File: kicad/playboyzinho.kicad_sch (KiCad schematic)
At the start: 17 parts, among them SW1 SW_Push, SW2 SW_Push, SW3 SW_Push, SW4 SW_Push, SW5 SW_Push, SW6 SW_Push, SW7 SW_Push, SW8 SW_Push, SW9 SW_SPDT, U1 esp32-s3-pl, U7 (amplificador)_MAX98357_Module

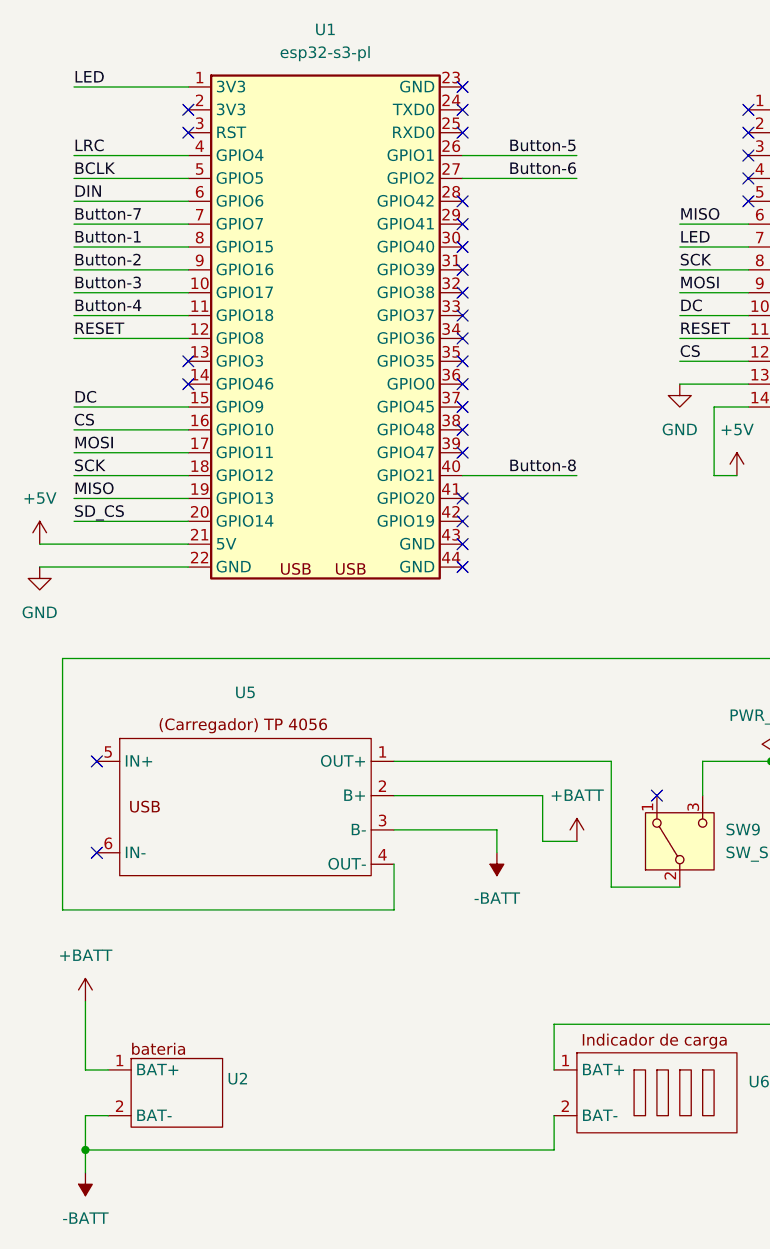
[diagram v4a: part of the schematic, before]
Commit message: refact: altera posição dos pinos dos botões e associa corretamente os footprints na parte de símbolos (antes, estava só no esquemático)
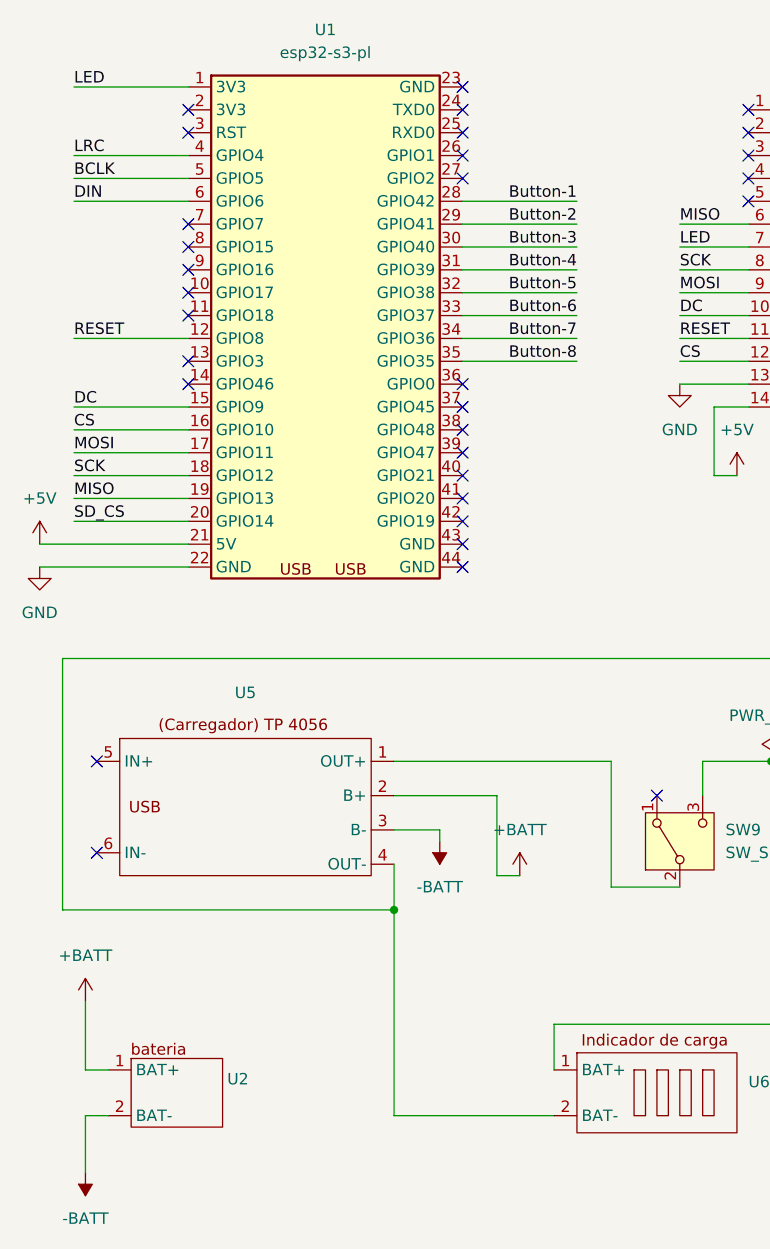
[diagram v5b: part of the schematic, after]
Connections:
- net -BATT: no longer U6.2 (BAT-)
- net Button-1: now also U1.28 (GPIO42); no longer U1.8 (GPIO15)
- net Button-2: now also U1.29 (GPIO41); no longer U1.9 (GPIO16)
- net Button-3: now also U1.30 (GPIO40); no longer U1.10 (GPIO17)
- net Button-4: now also U1.31 (GPIO39); no longer U1.11 (GPIO18)
- net Button-5: now also U1.32 (GPIO38); no longer U1.26 (GPIO1)
- net Button-6: now also U1.33 (GPIO37); no longer U1.27 (GPIO2)
- net Button-7: now also U1.34 (GPIO36); no longer U1.7 (GPIO7)
- net Button-8: now also U1.35 (GPIO35); no longer U1.40 (GPIO21)
- net at U3.4 (VIN-), U5.4 (OUT-): now also U6.2 (BAT-)

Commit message: feat: finaliza pcb
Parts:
- removed U6: (no value), lib-do-playboy:indicador-bateria, symbol lib-do-playboy:Indicador-Bateria
- added U6: (no value), lib-do-playboy:indicador-bateria, symbol lib-do-playboy:indicador-bateria
- U2: footprint (none) -> lib-do-playboy:bateria
- renumbered SW8 to SW1, SW7 to SW2, SW6 to SW3, SW5 to SW4, SW2 to SW5, SW1 to SW6, SW4 to SW7, SW3 to SW8
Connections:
- net +5V: now also U4.1 (VCC); no longer U4.14 (VCC)
- net BCLK: now also U1.19 (GPIO13); no longer U1.5 (GPIO5)
- net Button-1: now also SW1.1; no longer SW6.1
- net Button-2: now also SW2.1; no longer SW5.1
- net Button-3: now also SW3.1; no longer SW8.1
- net Button-4: now also SW4.1, U1.32 (GPIO38); no longer SW7.1, U1.31 (GPIO39)
- net Button-5: now also SW5.1, U1.31 (GPIO39); no longer SW4.1, U1.32 (GPIO38)
- net Button-6: now also SW6.1, U1.38 (GPIO48); no longer SW3.1, U1.33 (GPIO37)
- net Button-7: now also SW7.1, U1.40 (GPIO21); no longer SW2.1, U1.34 (GPIO36)
- net Button-8: now also SW8.1, U1.39 (GPIO47); no longer SW1.1, U1.35 (GPIO35)
- net CS: now also U1.17 (GPIO11), U4.3 (CS); no longer U1.16 (GPIO10), U4.12 (CS)
- net DC: now also U4.5 (DC); no longer U4.10 (DC)
- net DIN: now also U1.18 (GPIO12); no longer U1.6 (GPIO6)
- net GND: now also U1.23 (GND), U1.43 (GND), U1.44 (GND), U3.4 (VIN-), U4.2 (GND), U5.4 (OUT-), U6.2 (BAT-); no longer U4.13 (GND)
- net LRC: now also U1.20 (GPIO14); no longer U1.4 (GPIO4)
- net MISO: now also U1.9 (GPIO16), U4.9 (SDO-(MISO)); no longer U1.19 (GPIO13), U4.6 (SDO-(MISO))
- net MOSI: now also U1.12 (GPIO8), U4.6 (SDI-(MOSI)); no longer U1.17 (GPIO11), U4.9 (SDI-(MOSI))
- net RESET: now also U1.16 (GPIO10), U4.4 (RESET); no longer U1.12 (GPIO8), U4.11 (RESET)
- net SCK: now also U1.10 (GPIO17), U4.7 (SCK); no longer U1.18 (GPIO12), U4.8 (SCK)
- net SD_CS: now also U1.4 (GPIO4); no longer U1.20 (GPIO14)
- net at SW9.3 (C), U3.3 (VIN+): now also U6.1 (BAT+)
- net LED renamed 3V3
- net 3V3: now also U4.8 (LED); no longer U4.7 (LED)
- no-connect marks 35 -> 32
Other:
- moved on the sheet: LS1, U2, U3, U4, U5, U7

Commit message: fix: corrige indicador de bateria errado e faz pequenos ajustes
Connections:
- net GND: now also U6.1 (BAT-); no longer U6.2 (BAT-)
- net at SW9.3 (C), U3.3 (VIN+): now also U6.2 (BAT+); no longer U6.1 (BAT+)
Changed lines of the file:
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@@
 	)
 	(junction
-		(at 81.28 133.35)
-		(diameter 0)
-		(color 0 0 0 0)
-	)
-	(junction
 		(at 238.76 151.13)
 		(diameter 0)
@@
 		(color 0 0 0 0)
 	)
+	(junction
+		(at 81.28 147.32)
+		(diameter 0)
+		(color 0 0 0 0)
+	)
 	(no_connect
 		(at 54.61 48.26)
@@
 	(wire
 		(pts
-			(xy 95.25 142.24) (xy 137.16 142.24)
+			(xy 85.09 55.88) (xy 97.79 55.88)
 		)
 		(stroke
@@
 	(wire
 		(pts
-			(xy 85.09 55.88) (xy 97.79 55.88)
+			(xy 85.09 50.8) (xy 97.79 50.8)
 		)
 		(stroke
@@
 	(wire
 		(pts
-			(xy 85.09 50.8) (xy 97.79 50.8)
+			(xy 41.91 58.42) (xy 54.61 58.42)
 		)
 		(stroke
@@
 	(wire
 		(pts
-			(xy 41.91 58.42) (xy 54.61 58.42)
+			(xy 81.28 147.32) (xy 81.28 149.86)
 		)
 		(stroke
@@
 	(wire
 		(pts
-			(xy 81.28 133.35) (xy 87.63 133.35)
-		)
-		(stroke
-			(width 0)
-			(type default)
-		)
-	)
-	(wire
-		(pts
 			(xy 88.9 118.11) (xy 88.9 124.46)
 		)
@@
 	(wire
 		(pts
-			(xy 81.28 125.73) (xy 81.28 133.35)
+			(xy 81.28 125.73) (xy 81.28 147.32)
 		)
 		(stroke
@@
 	(wire
 		(pts
+			(xy 95.25 156.21) (xy 95.25 152.4)
+		)
+		(stroke
+			(width 0)
+			(type default)
+		)
+	)
+	(wire
+		(pts
 			(xy 270.51 151.13) (xy 270.51 138.43)
 		)
@@
 	(wire
 		(pts
+			(xy 81.28 147.32) (xy 95.25 147.32)
+		)
+		(stroke
+			(width 0)
+			(type default)
+		)
+	)
+	(wire
+		(pts
 			(xy 107.95 52.07) (xy 115.57 52.07)
 		)
@@
 	(wire
 		(pts
-			(xy 95.25 142.24) (xy 95.25 147.32)
-		)
-		(stroke
-			(width 0)
-			(type default)
-		)
-	)
-	(wire
-		(pts
 			(xy 111.76 113.03) (xy 119.38 113.03)
 		)
@@
 	(wire
 		(pts
-			(xy 87.63 133.35) (xy 87.63 152.4)
+			(xy 144.78 92.71) (xy 147.32 92.71)
 		)
 		(stroke
@@
 	(wire
 		(pts
-			(xy 144.78 92.71) (xy 147.32 92.71)
+			(xy 137.16 113.03) (xy 137.16 156.21)
 		)
 		(stroke
@@
 	(wire
 		(pts
-			(xy 137.16 142.24) (xy 137.16 113.03)
+			(xy 41.91 81.28) (xy 54.61 81.28)
 		)
 		(stroke
@@
 	(wire
 		(pts
-			(xy 41.91 81.28) (xy 54.61 81.28)
+			(xy 137.16 156.21) (xy 95.25 156.21)
 		)
 		(stroke
@@
 	(wire
 		(pts
-			(xy 87.63 152.4) (xy 95.25 152.4)
-		)
-		(stroke
-			(width 0)
-			(type default)
-		)
-	)
-	(wire
-		(pts
 			(xy 85.09 58.42) (xy 97.79 58.42)
 		)
@@
 	(symbol
 		(lib_id "power:GND")
-		(at 81.28 133.35 0)
+		(at 81.28 149.86 0)
 		(unit 1)
 		(body_style 1)
@@
 		(fields_autoplaced yes)
 		(property "Reference" "#PWR030"
-			(at 81.28 139.7 0)
+			(at 81.28 156.21 0)
 			(hide yes)
 			(show_name no)
@@
 		)
 		(property "Value" "GND"
-			(at 81.28 138.43 0)
+			(at 81.28 154.94 0)
 			(show_name no)
 			(do_not_autoplace no)
@@
 		)
 		(property "Footprint" ""
-			(at 81.28 133.35 0)
+			(at 81.28 149.86 0)
 			(hide yes)
 			(show_name no)
@@
 		)
 		(property "Datasheet" ""
-			(at 81.28 133.35 0)
+			(at 81.28 149.86 0)
 			(hide yes)
 			(show_name no)
@@
 		)
 		(property "Description" "Power symbol creates a global label with name \"GND\" , ground"
-			(at 81.28 133.35 0)
+			(at 81.28 149.86 0)
 			(hide yes)
 			(show_name no)
